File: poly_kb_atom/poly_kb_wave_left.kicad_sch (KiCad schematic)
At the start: 32 parts

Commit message: split kb prototype, left side
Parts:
- removed D?: D_Small, poly_kb:D_SOD-323Ext, symbol Device:D_Small
- removed TP? (x2): TestPoint_Flag, symbol Connector:TestPoint_Flag
- added D_ENC_1, D_ENC_2: D_Small, poly_kb:D_SOD-323Ext, symbol Device:D_Small
- added H1, H2, H3, H4, H5, H6: MountingHole_Pad, MountingHole:MountingHole_3mm_Pad_Via, symbol Mechanical:MountingHole_Pad
- added TP2: LED_ARR_END, TestPoint:TestPoint_Pad_D1.5mm, symbol Connector:TestPoint_Flag
- C_VBAT_1, C_VBAT_2, C_VBAT_3, C_VDD_1, C_VDD_2: renamed from C?; footprint (none) -> Capacitor_SMD:C_0603_1608Metric
- JP1: renamed from JP?; value SolderJumper_3_Open -> RX_SEL; footprint (none) -> Jumper:SolderJumper-3_P1.3mm_Open_RoundedPad1.0x1.5mm_NumberLabels
- JP2: renamed from JP?; value SolderJumper_3_Open -> TX_SEL; footprint (none) -> Jumper:SolderJumper-3_P1.3mm_Open_RoundedPad1.0x1.5mm_NumberLabels
- JP3: renamed from JP?; value SolderJumper_3_Open -> VCC_SEL; footprint (none) -> Jumper:SolderJumper-3_P1.3mm_Open_RoundedPad1.0x1.5mm_NumberLabels
- L_VBAT_1: renamed from L?; footprint (none) -> Inductor_SMD:L_7.3x7.3_H4.5
- OLED1: renamed from J?; footprint (none) -> poly_kb:SSD1306_OLED_DISPLAY_128X64_0-92INCH
- R1, R2, R3, R4, R_VBAT_1, R_VBAT_2, R_VDD_1: renamed from R?; footprint (none) -> Resistor_SMD:R_0603_1608Metric
- RESET1: renamed from RESET; footprint (none) -> Button_Switch_SMD:Panasonic_EVQPUK_EVQPUB
- SERIAL1: renamed from J?; footprint (none) -> poly_kb:MOLEX_85502-5007_6P6C_90DEG
- TP1: renamed from TP?; value TestPoint_Flag -> DISP_EN; footprint (none) -> TestPoint:TestPoint_Pad_D1.5mm
- TP3: renamed from TP?; value TestPoint_Flag -> VBAT; footprint (none) -> TestPoint:TestPoint_Pad_D1.5mm
- TP4: renamed from TP?; value TestPoint_Flag -> VDD; footprint (none) -> TestPoint:TestPoint_Pad_D1.5mm
- TP5: renamed from TP?; value TestPoint_Flag -> SR_CARRY; footprint (none) -> TestPoint:TestPoint_Pad_D1.5mm
- U1: renamed from U?; footprint RPi_Pico:RPi_Pico_SMD_TH -> poly_kb:RPi_Pico_SMD
- U_VBAT_1: renamed from U?; footprint (none) -> Package_TO_SOT_SMD:TSOT-23-5
- U_VDD_1: renamed from U?; footprint (none) -> Package_TO_SOT_SMD:SOT-23-5
- gave numbers to parts that had none: 3
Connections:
- net Col8: now also ENC1.C
- net GND: now also H1.1, H2.1, H3.1, H4.1, H5.1, H6.1
- net Row2: now also D_ENC_1.2 (A); no longer ENC1.A
- net Row3: now also D_ENC_2.2 (A); no longer ENC1.B
- net K_L5/LED_DOUT: now also TP2.1
- net RX: now reaches JP1.2 (C), SERIAL1.4
- net TX: now reaches JP2.2 (C), SERIAL1.3
- net 3V3 renamed VDD_DISP
- net 4V2 renamed VBAT_DISP
- net 5V renamed VBUS
- net ShiftRegisters/Carry renamed ShiftRegisters/CarryOut
- new net: D_ENC_2.1 (K), ENC1.B
- new net: D_ENC_1.1 (K), ENC1.A
- no-connect marks 8 -> 10
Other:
- sheet sheet605ED2EB renamed K_L1
- sheet sheet605ED2EB1 renamed K_1
- sheet sheet605ED2EB10 renamed K_W
- sheet sheet605ED2EB11 renamed K_E
- sheet sheet605ED2EB12 renamed K_Q
- sheet sheet605ED2EB13 renamed K_L2
- sheet sheet605ED2EB14 renamed K_L8
- sheet sheet605ED2EB15 renamed K_G
- sheet sheet605ED2EB16 renamed K_F
- sheet sheet605ED2EB17 renamed K_S
- sheet sheet605ED2EB18 renamed K_D
- sheet sheet605ED2EB19 renamed K_A
- sheet sheet605ED2EB2 renamed K_2
- sheet sheet605ED2EB20 renamed K_L3
- sheet sheet605ED2EB21 renamed K_L9
- sheet sheet605ED2EB23 renamed K_V
- sheet sheet605ED2EB24 renamed K_X
- sheet sheet605ED2EB25 renamed K_C
- sheet sheet605ED2EB26 renamed K_Z
- sheet sheet605ED2EB27 renamed K_L4
- sheet sheet605ED2EB28 renamed K_B6
- sheet sheet605ED2EB29 renamed K_B5
- sheet sheet605ED2EB3 renamed K_3
- sheet sheet605ED2EB30 renamed K_B4
- sheet sheet605ED2EB31 renamed K_B2
- sheet sheet605ED2EB32 renamed K_B3
- sheet sheet605ED2EB33 renamed K_B1
- sheet sheet605ED2EB34 renamed K_L5
- sheet sheet605ED2EB35 renamed K_B7
- sheet sheet605ED2EB4 renamed K_4
- sheet sheet605ED2EB5 renamed K_5
- sheet sheet605ED2EB6 renamed K_L6
- sheet sheet605ED2EB7 renamed K_L7
- sheet sheet605ED2EB8 renamed K_T
- sheet sheet605ED2EB9 renamed K_R
- removed sheet sheet605ED2EB22
- added sheet K_B (SSD1306_TO_SPI.kicad_sch)
- sheet K_1 ports: added VBAT, VDD, VLED; removed 3V3, 4V2, 5V
- sheet K_2 ports: added VBAT, VDD, VLED; removed 3V3, 4V2, 5V
- sheet K_3 ports: added VBAT, VDD, VLED; removed 3V3, 4V2, 5V
- sheet K_4 ports: added VBAT, VDD, VLED; removed 3V3, 4V2, 5V
- sheet K_5 ports: added VBAT, VDD, VLED; removed 3V3, 4V2, 5V
- sheet K_A ports: added VBAT, VDD, VLED; removed 3V3, 4V2, 5V
- sheet K_B1 ports: added VBAT, VDD, VLED; removed 3V3, 4V2, 5V
- sheet K_B2 ports: added VBAT, VDD, VLED; removed 3V3, 4V2, 5V
- sheet K_B3 ports: added VBAT, VDD, VLED; removed 3V3, 4V2, 5V
- sheet K_B4 ports: added VBAT, VDD, VLED; removed 3V3, 4V2, 5V
- sheet K_B5 ports: added VBAT, VDD, VLED; removed 3V3, 4V2, 5V
- sheet K_B6 ports: added VBAT, VDD, VLED; removed 3V3, 4V2, 5V
- sheet K_B7 ports: added VBAT, VDD, VLED; removed 3V3, 4V2, 5V
- sheet K_C ports: added VBAT, VDD, VLED; removed 3V3, 4V2, 5V
- sheet K_D ports: added VBAT, VDD, VLED; removed 3V3, 4V2, 5V
- sheet K_E ports: added VBAT, VDD, VLED; removed 3V3, 4V2, 5V
- sheet K_F ports: added VBAT, VDD, VLED; removed 3V3, 4V2, 5V
- sheet K_G ports: added VBAT, VDD, VLED; removed 3V3, 4V2, 5V
- sheet K_L1 ports: added VBAT, VDD, VLED; removed 3V3, 4V2, 5V
- sheet K_L2 ports: added VBAT, VDD, VLED; removed 3V3, 4V2, 5V
- sheet K_L3 ports: added VBAT, VDD, VLED; removed 3V3, 4V2, 5V
- sheet K_L4 ports: added VBAT, VDD, VLED; removed 3V3, 4V2, 5V
- sheet K_L5 ports: added VBAT, VDD, VLED; removed 3V3, 4V2, 5V
- sheet K_L6 ports: added VBAT, VDD, VLED; removed 3V3, 4V2, 5V
- sheet K_L7 ports: added VBAT, VDD, VLED; removed 3V3, 4V2, 5V
- sheet K_L8 ports: added VBAT, VDD, VLED; removed 3V3, 4V2, 5V
- sheet K_L9 ports: added VBAT, VDD, VLED; removed 3V3, 4V2, 5V
- sheet K_Q ports: added VBAT, VDD, VLED; removed 3V3, 4V2, 5V
- sheet K_R ports: added VBAT, VDD, VLED; removed 3V3, 4V2, 5V
- sheet K_S ports: added VBAT, VDD, VLED; removed 3V3, 4V2, 5V
- sheet K_T ports: added VBAT, VDD, VLED; removed 3V3, 4V2, 5V
- sheet K_V ports: added VBAT, VDD, VLED; removed 3V3, 4V2, 5V
- sheet K_W ports: added VBAT, VDD, VLED; removed 3V3, 4V2, 5V
- sheet K_X ports: added VBAT, VDD, VLED; removed 3V3, 4V2, 5V
- sheet K_Z ports: added VBAT, VDD, VLED; removed 3V3, 4V2, 5V
- sheet ShiftRegisters ports: added CarryOut, MReset; removed Carry, Reset

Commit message: almost finished wave
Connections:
- net K_L5/LED_DOUT is gone; now on net K_B1/LED_DOUT: TP2.1
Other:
- removed sheet K_L5
- added sheet K_B8 (SSD1306_TO_SPI.kicad_sch)

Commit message: Final version of wave
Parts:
- added H7, H8: (no value), symbol Mechanical:MountingHole_Pad
- added TP10, TP11, TP12, TP6, TP7, TP8, TP9: (no value), symbol Connector:TestPoint_Flag
- C_VBAT_1, C_VBAT_3, C_VDD_1, C_VDD_2: value 10uF -> (none); footprint Capacitor_SMD:C_0603_1608Metric -> (none); LCSC (none) -> C96446
- C_VBAT_2: value 22pF -> (none); footprint Capacitor_SMD:C_0603_1608Metric -> (none); LCSC (none) -> C1653
- D_ARR_1, D_ENC_1, D_ENC_2, D_ENC_3: value D_Small -> (none); footprint poly_kb:D_SOD-323Ext -> (none)
- ENC1: value RotaryEncoder_Switch -> (none); footprint KUSOboard:EVQWGD001 -> (none)
- H1, H2, H3, H4, H5, H6: value MountingHole_Pad -> (none); footprint MountingHole:MountingHole_3mm_Pad_Via -> (none)
- JP1: value RX_SEL -> (none); footprint Jumper:SolderJumper-3_P1.3mm_Open_RoundedPad1.0x1.5mm_NumberLabels -> (none)
- JP2: value TX_SEL -> (none); footprint Jumper:SolderJumper-3_P1.3mm_Open_RoundedPad1.0x1.5mm_NumberLabels -> (none)
- JP3: value VCC_SEL -> (none); footprint Jumper:SolderJumper-3_P1.3mm_Open_RoundedPad1.0x1.5mm_NumberLabels -> (none)
- L_VBAT_1: value 3.3uH -> (none); footprint Inductor_SMD:L_7.3x7.3_H4.5 -> (none); LCSC (none) -> C2045449
- OLED1: value OPT_OLED_DISPLAY -> (none); footprint poly_kb:SSD1306_OLED_DISPLAY_128X64_0-92INCH -> (none)
- R1, R2, R3, R4: value 10k -> (none); footprint Resistor_SMD:R_0603_1608Metric -> (none); LCSC (none) -> C25804
- RESET1: value SW_Push -> (none); footprint Button_Switch_SMD:Panasonic_EVQPUK_EVQPUB -> (none); LCSC (none) -> C526225
- R_VBAT_1: value 820k -> (none); footprint Resistor_SMD:R_0603_1608Metric -> (none); LCSC (none) -> C23252
- R_VBAT_2: value 150k -> (none); footprint Resistor_SMD:R_0603_1608Metric -> (none); LCSC (none) -> C22807
- R_VDD_1: value 22k -> (none); footprint Resistor_SMD:R_0603_1608Metric -> (none); LCSC (none) -> C31850
- SERIAL1: value RJ12 -> (none); footprint poly_kb:MOLEX_85502-5007_6P6C_90DEG -> (none)
- TP1: value DISP_EN -> (none); footprint TestPoint:TestPoint_Pad_D1.5mm -> (none)
- TP2: value LED_ARR_END -> (none); footprint TestPoint:TestPoint_Pad_D1.5mm -> (none)
- TP3: value VBAT -> (none); footprint TestPoint:TestPoint_Pad_D1.5mm -> (none)
- TP4: value VDD -> (none); footprint TestPoint:TestPoint_Pad_D1.5mm -> (none)
- TP5: value SR_CARRY -> (none); footprint TestPoint:TestPoint_Pad_D1.5mm -> (none)
- U1: value Pico -> (none); footprint poly_kb:RPi_Pico_SMD -> (none)
- U_VBAT_1: value TD6811 -> (none); footprint Package_TO_SOT_SMD:TSOT-23-5 -> (none); LCSC (none) -> C189486
- U_VDD_1: value MT9700 -> (none); footprint Package_TO_SOT_SMD:SOT-23-5 -> (none); LCSC (none) -> C89855
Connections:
- net D-C: now also TP11.1
- net GND: now also H7.1, H8.1
- net RESET: now also TP12.1
- net SCLK: now also TP7.1
- net SDIN: now also TP9.1
- net SR_CLOCK: now also TP8.1
- net SR_DATA: now also TP10.1
- net SR_LATCH: now also TP6.1

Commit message: Added power leds
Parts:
- added D_BAT_1, D_BAT_2: (no value), symbol Device:LED_Small
- added R_VBAT_1'1, R_VBAT_3, R_VDD_2: (no value), symbol Device:R_Small
- C_VBAT_1, C_VBAT_3, C_VDD_1, C_VDD_2: JLC (none) -> 0805; LCSC C96446 -> C15850
- C_VBAT_2, R1, R2, R3, R4, R_VBAT_2, R_VDD_1: JLC (none) -> 0603
- D_ARR_1: JLC (none) -> D_SOD-323Ext; LCSC C169468 -> C2128
- D_ENC_1, D_ENC_2, D_ENC_3: JLC (none) -> 0805; LCSC C169468 -> C2128
- L_VBAT_1: JLC (none) -> L_PANASONIC_ELT5KT; LCSC C2045449 -> C2836880
- RESET1: JLC (none) -> Panasonic_EVQPUK_EVQPUB
- R_VBAT_1: JLC (none) -> 0603; LCSC C23252 -> C23150
- U_VBAT_1: JLC (none) -> TSOT-23-5
- U_VDD_1: JLC (none) -> SOT-23-5
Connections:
- net GND: now also R_VBAT_3.1, R_VDD_2.1
- net VBAT_DISP: now also D_BAT_1.2 (A)
- net VDD_DISP: now also D_BAT_2.2 (A)
- net at C_VBAT_2.2, R_VBAT_2.2, U_VBAT_1.5 (FB): now also R_VBAT_1'1.1; no longer R_VBAT_1.1
- new net: D_BAT_2.1 (K), R_VDD_2.2
- new net: R_VBAT_1'1.2, R_VBAT_1.1
- new net: D_BAT_1.1 (K), R_VBAT_3.2
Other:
- note added: "3.72V"
- note removed: "3.88V"
- moved on the sheet: R_VBAT_2

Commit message: Updated WaveL to Revision 1.1
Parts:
- removed D_ARR_1: (no value), symbol Device:D_Small
- removed JP3: (no value), symbol Jumper:SolderJumper_3_Open
- removed TP1: (no value), symbol Connector:TestPoint_Flag
- C_VBAT_1, C_VBAT_3, C_VDD_1, C_VDD_2: value (none) -> 10uF; footprint (none) -> Capacitor_SMD:C_0805_2012Metric
- C_VBAT_2: value (none) -> 22pF; footprint (none) -> Capacitor_SMD:C_0603_1608Metric
- D5: renamed from D_BAT_2; value (none) -> Blue; footprint (none) -> LED_SMD:LED_0805_2012Metric
- D6: renamed from D_BAT_1; value (none) -> Yellow; footprint (none) -> LED_SMD:LED_0805_2012Metric
- D_ENC_1, D_ENC_2, D_ENC_3: value (none) -> D_Small; footprint (none) -> poly_kb:D_SOD-323Ext
- ENC1: value (none) -> RotaryEncoder_Switch; footprint (none) -> KUSOboard:EVQWGD001
- H1, H2, H3, H4, H5, H6, H7, H8: value (none) -> MountingHole_Pad; footprint (none) -> MountingHole:MountingHole_3mm_Pad_Via
- JP1: value (none) -> RX_SEL; footprint (none) -> Jumper:SolderJumper-3_P1.3mm_Open_RoundedPad1.0x1.5mm_NumberLabels
- JP2: value (none) -> TX_SEL; footprint (none) -> Jumper:SolderJumper-3_P1.3mm_Open_RoundedPad1.0x1.5mm_NumberLabels
- L_VBAT_1: value (none) -> 4.7uH; footprint (none) -> poly_kb:MCS0530-4R7MN2
- OLED1: value (none) -> OPT_OLED_DISPLAY; footprint (none) -> poly_kb:SSD1306_THT_OLED_DISPLAY_128X64_0-92INCH
- R1, R2, R3, R4: value (none) -> 10k; footprint (none) -> Resistor_SMD:R_0603_1608Metric
- R5: renamed from R_VDD_2; value (none) -> 1k; footprint (none) -> Resistor_SMD:R_0603_1608Metric
- R6: renamed from R_VBAT_3; value (none) -> 1k; footprint (none) -> Resistor_SMD:R_0603_1608Metric
- RESET1: value (none) -> SW_Push; footprint (none) -> Button_Switch_SMD:Panasonic_EVQPUK_EVQPUB
- R_VBAT_1, R_VBAT_1'1: value (none) -> 390k; footprint (none) -> Resistor_SMD:R_0603_1608Metric
- R_VBAT_2: value (none) -> 150k; footprint (none) -> Resistor_SMD:R_0603_1608Metric
- R_VDD_1: value (none) -> 22k; footprint (none) -> Resistor_SMD:R_0603_1608Metric
- SERIAL1: value (none) -> RJ12; footprint (none) -> poly_kb:MOLEX_85502-5007_6P6C_90DEG
- TP10: value (none) -> SR_DATA; footprint (none) -> TestPoint:TestPoint_Pad_D1.5mm
- TP11: value (none) -> D-C; footprint (none) -> TestPoint:TestPoint_Pad_D1.5mm
- TP12: value (none) -> RESET; footprint (none) -> TestPoint:TestPoint_Pad_D1.5mm
- TP2: value (none) -> LED_ARR_END; footprint (none) -> TestPoint:TestPoint_Pad_D1.5mm
- TP3: value (none) -> VBAT; footprint (none) -> TestPoint:TestPoint_Pad_D1.5mm
- TP4: value (none) -> VDD; footprint (none) -> TestPoint:TestPoint_Pad_D1.5mm
- TP5: value (none) -> SR_CARRY; footprint (none) -> TestPoint:TestPoint_Pad_D1.5mm
- TP6: value (none) -> SR_LATCH; footprint (none) -> TestPoint:TestPoint_Pad_D1.5mm
- TP7: value (none) -> SDIN; footprint (none) -> TestPoint:TestPoint_Pad_D1.5mm
- TP8: value (none) -> SR_CLOCK; footprint (none) -> TestPoint:TestPoint_Pad_D1.5mm
- TP9: value (none) -> SCLK; footprint (none) -> TestPoint:TestPoint_Pad_D1.5mm
- U1: value (none) -> Pico; footprint (none) -> poly_kb:RPi_Pico_SMD
- U_VBAT_1: value (none) -> TD6811; footprint (none) -> Package_TO_SOT_SMD:TSOT-23-5
- U_VDD_1: value (none) -> MT9700; footprint (none) -> Package_TO_SOT_SMD:SOT-23-5
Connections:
- net Col8: now also U1.5 (GPIO3); no longer U1.22 (GPIO17)
- net GND: now also OLED1.1 (Pin_1); no longer OLED1.4 (Pin_4)
- net I2C_SCK: now also OLED1.3 (Pin_3); no longer OLED1.2 (Pin_2)
- net I2C_SDA: now also OLED1.4 (Pin_4); no longer OLED1.1 (Pin_1)
- net PICO_3V3: now also OLED1.2 (Pin_2), U_VBAT_1.1 (RUN), U_VDD_1.4 (EN); no longer OLED1.3 (Pin_3)
- net SCLK: now also R2.2, TP9.1; no longer R3.2, TP7.1
- net SDIN: now also R3.2, TP7.1; no longer R2.2, TP9.1
- removed net DispEN: U1.5 (GPIO3), U_VBAT_1.1 (RUN), U_VDD_1.4 (EN)
- new net SPI0_CS_NC: U1.22 (GPIO17)
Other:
- title: (none) -> Poly Keyboard Wave L
- moved on the sheet: D6, OLED1, R2, R3, R6, TP7, TP9

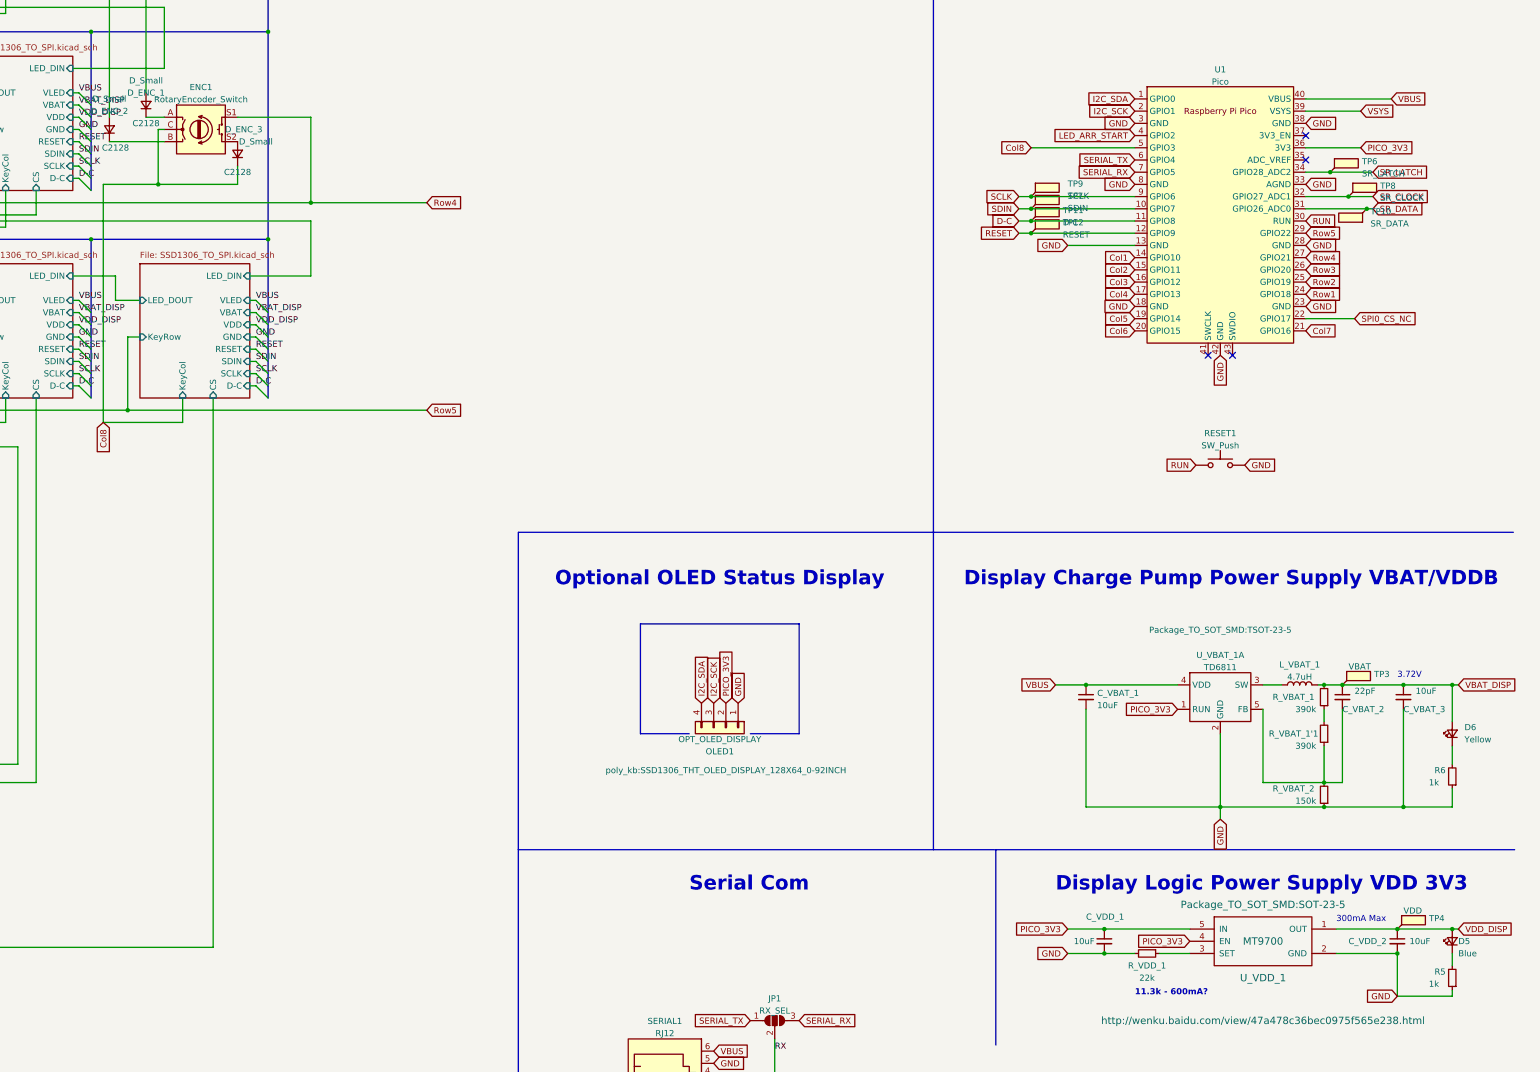
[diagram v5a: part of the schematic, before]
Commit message: Updated changes made in produced PCB
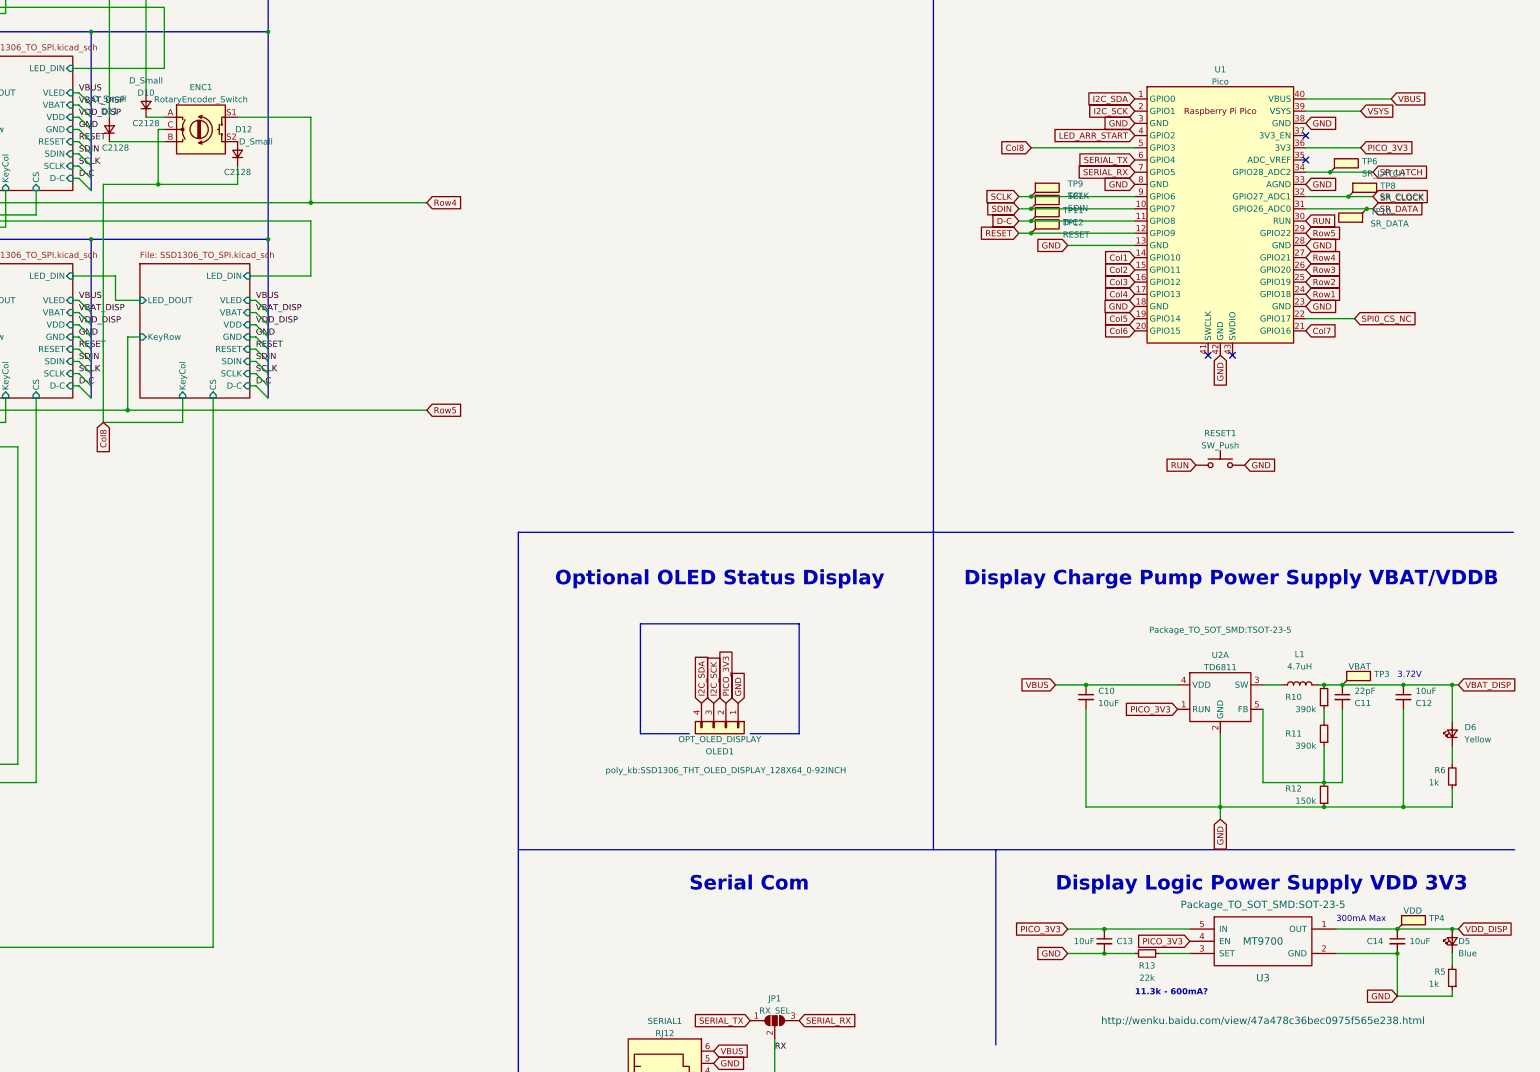
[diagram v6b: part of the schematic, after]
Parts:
- renumbered C_VBAT_1 to C10, C_VBAT_2 to C11, C_VBAT_3 to C12, C_VDD_1 to C13, C_VDD_2 to C14, D_ENC_1 to D10, D_ENC_2 to D11, D_ENC_3 to D12, L_VBAT_1 to L1, R_VBAT_1 to R10, R_VBAT_1'1 to R11, R_VBAT_2 to R12, R_VDD_1 to R13, U_VBAT_1 to U2, U_VDD_1 to U3

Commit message: More cleanup of the left side (wave), added alps ec11 compatiblity
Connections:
- net RX is gone; now on net SERIAL_RX: JP1.2 (C), SERIAL1.4
- net TX is gone; now on net SERIAL_TX: JP2.2 (C), SERIAL1.3
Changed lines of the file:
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@@
   (junction (at 285.75 208.28) (diameter 0) (color 0 0 0 0)
   )
+  (junction (at 427.99 382.27) (diameter 0) (color 0 0 0 0)
+  )
   (junction (at 322.58 208.28) (diameter 0) (color 0 0 0 0)
   )
@@
   (junction (at 332.74 397.51) (diameter 0) (color 0 0 0 0)
   )
+  (junction (at 422.91 384.81) (diameter 0) (color 0 0 0 0)
+  )
   (junction (at 358.14 397.51) (diameter 0) (color 0 0 0 0)
   )
@@
     (stroke (width 0) (type default) (color 0 0 0 0))
   )
+  (wire (pts (xy 433.07 370.84) (xy 433.07 382.27))
+    (stroke (width 0) (type default) (color 0 0 0 0))
+  )
   (wire (pts (xy 148.59 88.9) (xy 143.51 88.9))
     (stroke (width 0) (type default) (color 0 0 0 0))
@@
     (stroke (width 0) (type default) (color 0 0 0 0))
   )
+  (wire (pts (xy 422.91 384.81) (xy 422.91 396.24))
+    (stroke (width 0) (type default) (color 0 0 0 0))
+  )
   (bus (pts (xy 212.09 93.98) (xy 212.09 91.44))
     (stroke (width 0) (type default) (color 0 0 0 0))
@@
     (stroke (width 0) (type default) (color 0 0 0 0))
   )
+  (wire (pts (xy 433.07 382.27) (xy 427.99 382.27))
+    (stroke (width 0) (type default) (color 0 0 0 0))
+  )
   (wire (pts (xy 213.36 71.12) (xy 237.49 71.12))
     (stroke (width 0) (type default) (color 0 0 0 0))
@@
     (stroke (width 0) (type default) (color 0 0 0 0))
   )
+  (wire (pts (xy 422.91 384.81) (xy 415.29 384.81))
+    (stroke (width 0) (type default) (color 0 0 0 0))
+  )
   (wire (pts (xy 281.94 226.06) (xy 283.21 226.06))
     (stroke (width 0) (type default) (color 0 0 0 0))
@@
     (stroke (width 0) (type default) (color 0 0 0 0))
   )
-  (wire (pts (xy 427.99 384.81) (xy 415.29 384.81))
+  (wire (pts (xy 427.99 384.81) (xy 422.91 384.81))
     (stroke (width 0) (type default) (color 0 0 0 0))
   )
